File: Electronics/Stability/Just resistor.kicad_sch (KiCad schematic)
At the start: 7 parts

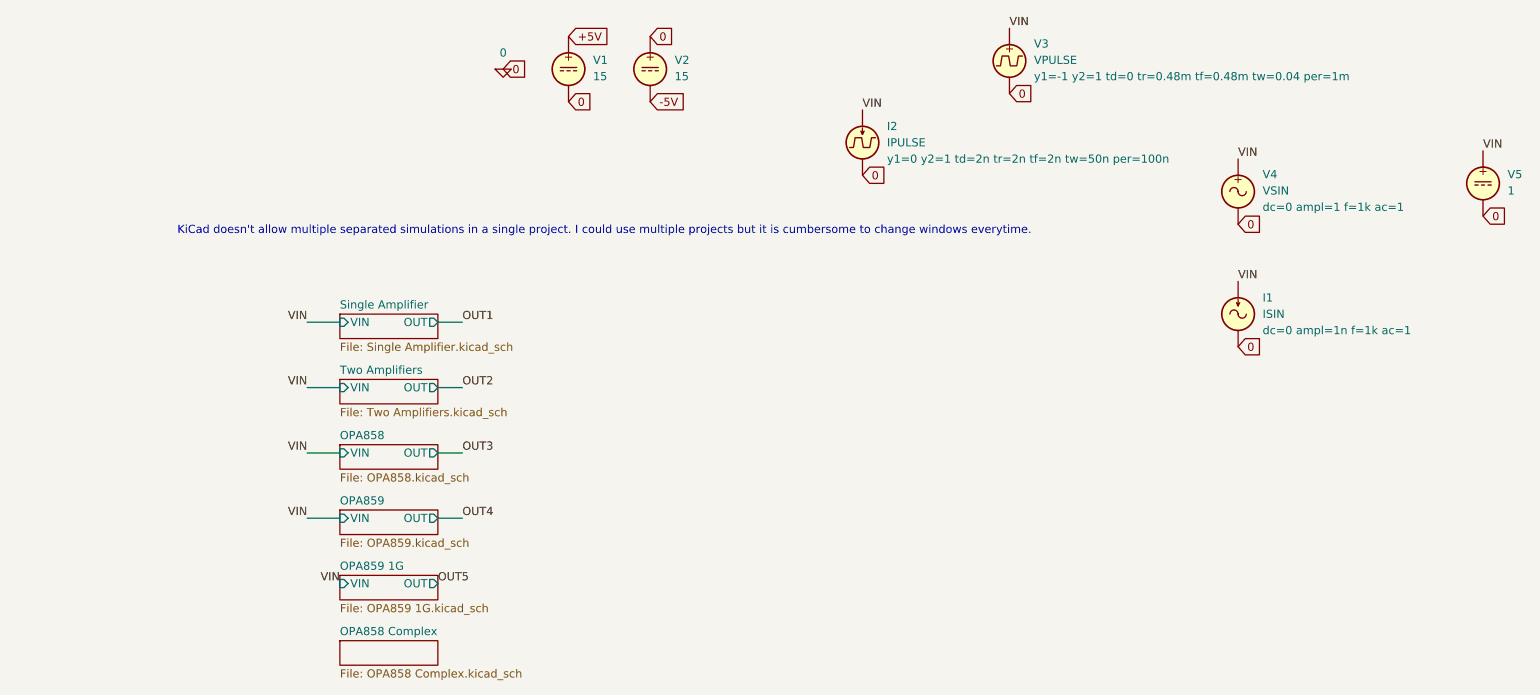
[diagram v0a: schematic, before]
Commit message: Create simpler stability simulation
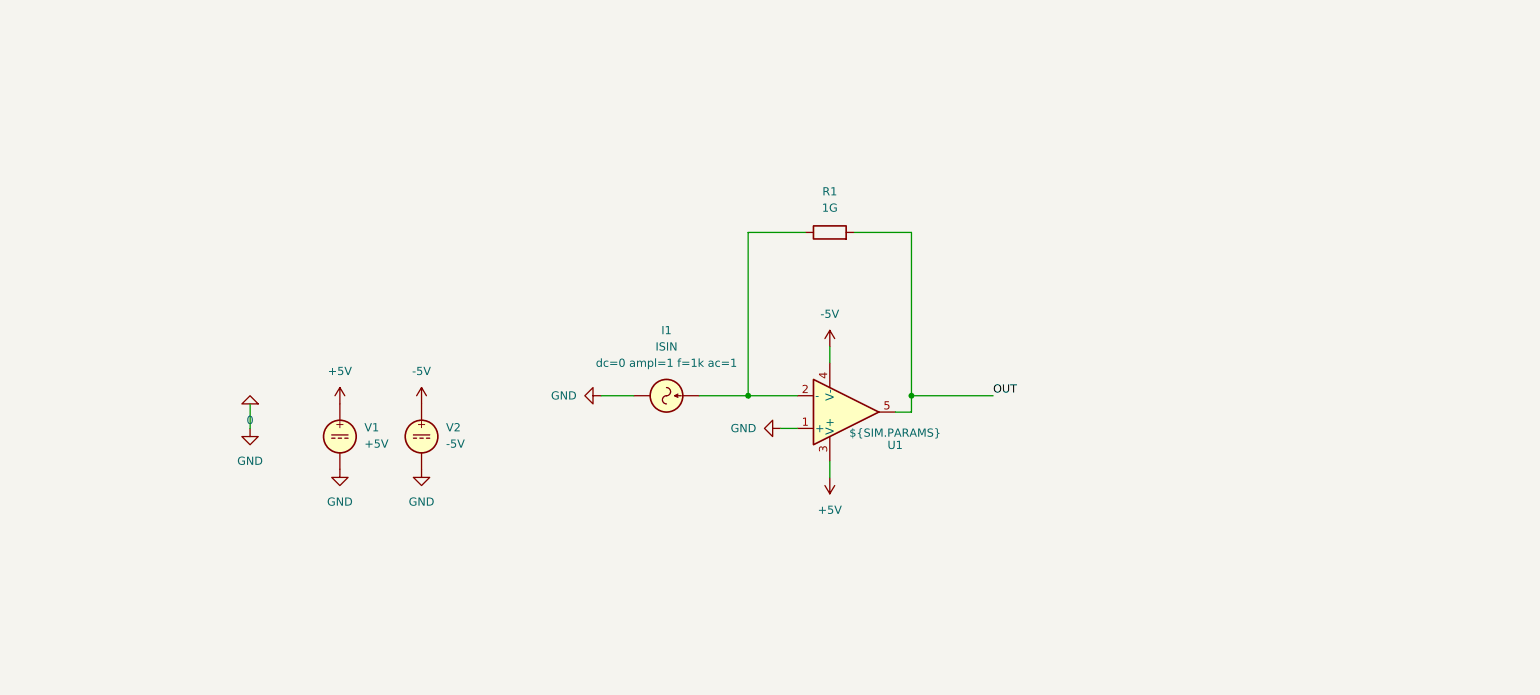
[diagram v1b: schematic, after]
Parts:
- removed I2: IPULSE, symbol Simulation_SPICE:IPULSE
- removed V3: VPULSE, symbol Simulation_SPICE:VPULSE
- removed V4: VSIN, symbol Simulation_SPICE:VSIN
- removed V5: 1, symbol Simulation_SPICE:VDC
- added R1: 1G, symbol Device:R
- added U1: ${SIM.PARAMS}, symbol Simulation_SPICE:OPAMP
- V1: value 15 -> +5V
- V2: value 15 -> -5V
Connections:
- net +5V: now also U1.3 (V+)
- net -5V: now also V2.1, U1.4 (V-); no longer V2.2
- net 0: now also V2.2, U1.1 (+); no longer V2.1
- net VIN: no longer names the net of I1.1
- net VIN: now also R1.1, U1.2 (-)
- new net OUT: R1.2, U1.5
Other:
- removed sheet OPA858
- removed sheet OPA858 Complex
- removed sheet OPA859
- removed sheet OPA859 1G
- removed sheet Single Amplifier
- removed sheet Two Amplifiers
- note removed: "KiCad doesn't allow multiple separated simulations in a single project. I could use multiple projects but it is cumbersome to change windows everytime."
